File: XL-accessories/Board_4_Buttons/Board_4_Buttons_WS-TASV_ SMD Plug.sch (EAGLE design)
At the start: 5 parts, among them J2 691709710305

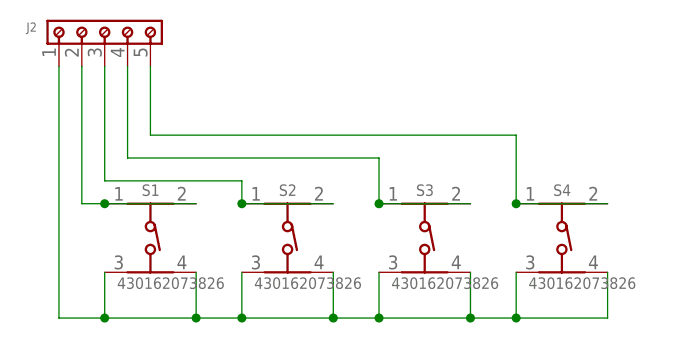
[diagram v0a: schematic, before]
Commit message: Update package and device set information for WS-TASV SMD Plug.
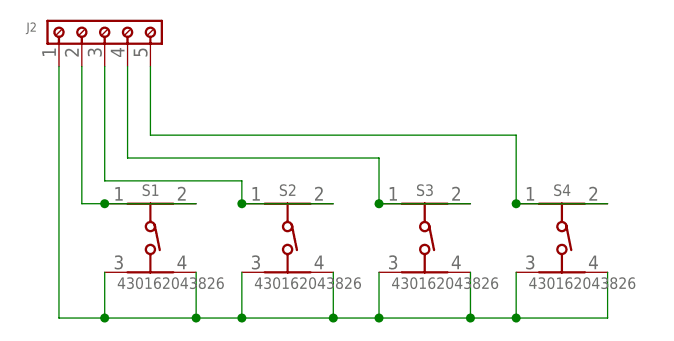
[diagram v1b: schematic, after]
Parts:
- S1, S2, S3, S4: value 430162073826 -> 430162043826; device Wurth_Switch_WS-TASV:430162073826 -> Wurth_Switch_WS-TASV:430162043826
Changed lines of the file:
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@@
 </classes>
 <parts>
-<part name="S1" library="Wurth_Switch_WS-TASV" library_urn="urn:adsk.eagle:library:18304196" deviceset="430162073826" device="" package3d_urn="urn:adsk.eagle:package:18304357/2" value="430162073826"/>
-<part name="S2" library="Wurth_Switch_WS-TASV" library_urn="urn:adsk.eagle:library:18304196" deviceset="430162073826" device="" package3d_urn="urn:adsk.eagle:package:18304357/2" value="430162073826"/>
-<part name="S3" library="Wurth_Switch_WS-TASV" library_urn="urn:adsk.eagle:library:18304196" deviceset="430162073826" device="" package3d_urn="urn:adsk.eagle:package:18304357/2" value="430162073826"/>
-<part name="S4" library="Wurth_Switch_WS-TASV" library_urn="urn:adsk.eagle:library:18304196" deviceset="430162073826" device="" package3d_urn="urn:adsk.eagle:package:18304357/2" value="430162073826"/>
+<part name="S1" library="Wurth_Switch_WS-TASV" library_urn="urn:adsk.eagle:library:18304196" deviceset="430162043826" device="" package3d_urn="urn:adsk.eagle:package:18304303/2" value="430162043826"/>
+<part name="S2" library="Wurth_Switch_WS-TASV" library_urn="urn:adsk.eagle:library:18304196" deviceset="430162043826" device="" package3d_urn="urn:adsk.eagle:package:18304303/2" value="430162043826"/>
+<part name="S3" library="Wurth_Switch_WS-TASV" library_urn="urn:adsk.eagle:library:18304196" deviceset="430162043826" device="" package3d_urn="urn:adsk.eagle:package:18304303/2" value="430162043826"/>
+<part name="S4" library="Wurth_Switch_WS-TASV" library_urn="urn:adsk.eagle:library:18304196" deviceset="430162043826" device="" package3d_urn="urn:adsk.eagle:package:18304303/2" value="430162043826"/>
 <part name="J2" library="Wurth_Connectors_WR-TBL Rising Cage Clamp" library_urn="urn:adsk.eagle:library:16280519" deviceset="691709710305" device="" package3d_urn="urn:adsk.eagle:package:16248446/4" value="691709710305"/>
 </parts>
